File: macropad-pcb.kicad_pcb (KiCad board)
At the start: 2 copper layers, 75 x 35 mm, 12 parts

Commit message: rev2 ready for sleeping on
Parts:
- removed G***: LOGO, ct-kicad:awesome-logo
- removed MAIN: HC-FPC-05-10-16RLTAG, ct-kicad:FPC-SMD_16P-P0.50_HCTL_HC-FPC-05-10-16RLTAG
- added J1: Conn_01x01_Socket, Connector_PinHeader_2.54mm:PinHeader_1x01_P2.54mm_Vertical, F.Cu at (176.9, 106.0)
- added J10: Conn_01x01_Socket, Connector_PinHeader_2.54mm:PinHeader_1x01_P2.54mm_Vertical, F.Cu at (144.3, 102.8)
- added J2: Conn_01x01_Socket, Connector_PinHeader_2.54mm:PinHeader_1x01_P2.54mm_Vertical, F.Cu at (157.6, 102.2)
- added J3: Conn_01x01_Socket, Connector_PinHeader_2.54mm:PinHeader_1x01_P2.54mm_Vertical, F.Cu at (136.0, 102.0)
- added J4: Conn_01x01_Socket, Connector_PinHeader_2.54mm:PinHeader_1x01_P2.54mm_Vertical, F.Cu at (121.5, 102.0)
- added J5: Conn_01x01_Socket, Connector_PinHeader_2.54mm:PinHeader_1x01_P2.54mm_Vertical, F.Cu at (151.7, 102.8)
- added J6: Conn_01x01_Socket, Connector_PinHeader_2.54mm:PinHeader_1x01_P2.54mm_Vertical, F.Cu at (117.5, 96.5)
- added J7: Conn_01x01_Socket, Connector_PinHeader_2.54mm:PinHeader_1x01_P2.54mm_Vertical, F.Cu at (117.5, 103.4)
- added J8: Conn_01x01_Socket, Connector_PinHeader_2.54mm:PinHeader_1x01_P2.54mm_Vertical, F.Cu at (175.8, 94.8)
- added J9: Conn_01x01_Socket, Connector_PinHeader_2.54mm:PinHeader_1x01_P2.54mm_Vertical, F.Cu at (148.0, 102.8)
- added LOGO1: **REF, ct-kicad:awesome-logo, F.Cu at (140.6, 99.3)
- added LOGO2: **REF, ct-kicad:qmk-lite, B.Cu at (147.8, 100.0)
- added MAIN1: HC-FPC-05-10-16RLTAG, ct-kicad:FPC-SMD_16P-P0.50_HCTL_HC-FPC-05-10-16RLTAG, F.Cu at (174.0, 100.0)
- H1, H2: footprint MountingHole:MountingHole_3mm -> MountingHole:MountingHole_3mm_Pad_Via
- moved R9C8 90.0 mm to (174.3, 110.9), turned to 90 degrees
- moved R8C8 90.0 mm to (174.3, 88.9), turned to 90 degrees
- moved R9C11 76.1 mm to (120.3, 110.9), turned to 90 degrees
- moved R8C11 75.7 mm to (120.3, 88.9), turned to 90 degrees
- moved R8C9 64.9 mm to (156.3, 88.9), turned to 90 degrees
- moved R9C9 64.9 mm to (156.3, 110.9), turned to 90 degrees
- moved R9C10 58.5 mm to (138.3, 110.9), turned to 90 degrees
- moved H1 58.5 mm to (130.0, 100.0)
- moved H2 58.5 mm to (165.0, 100.0)
- moved R8C10 58.4 mm to (138.3, 88.9), turned to 90 degrees
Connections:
- R8C10 pad 1: Net-(P3-Pad11) -> row8
- R8C10 pad 10: GND -> VCC
- R8C10 pad 11: Net-(P5-Pad11) -> VCC
- R8C10 pad 12: col10 -> VCC
- R8C10 pad 13: row8 -> Net-(R8C10-Pad13)
- R8C10 pad 14: unconnected-(P5-Pad14) -> GND
- R8C10 pad 15: unconnected-(P5-Pad15) -> GND
- R8C10 pad 2: VCC -> col10
- R8C10 pad 3: VCC -> Net-(R8C10-Pad3)
- R8C10 pad 4: VCC -> GND
- R8C10 pad 5: VCC -> GND
- R8C10 pad 9: GND -> VCC
- R8C11 pad 1: Net-(P5-Pad11) -> row8
- R8C11 pad 10: GND -> VCC
- R8C11 pad 11: from_row_9_DO -> VCC
- R8C11 pad 12: col11 -> VCC
- R8C11 pad 13: row8 -> Net-(R8C10-Pad3)
- R8C11 pad 14: unconnected-(P7-Pad14) -> GND
- R8C11 pad 15: unconnected-(P7-Pad15) -> GND
- R8C11 pad 2: VCC -> col11
- R8C11 pad 3: VCC -> from_row_9_DO
- R8C11 pad 4: VCC -> GND
- R8C11 pad 5: VCC -> GND
- R8C11 pad 9: GND -> VCC
- R8C8 pad 1: Net-(P1-Pad1) -> row8
- R8C8 pad 10: GND -> VCC
- R8C8 pad 11: Net-(P1-Pad11) -> VCC
- R8C8 pad 12: col8 -> VCC
- R8C8 pad 13: row8 -> LED_DI
- R8C8 pad 14: unconnected-(P1-Pad14) -> GND
- R8C8 pad 15: unconnected-(P1-Pad15) -> GND
- R8C8 pad 2: VCC -> col8
- R8C8 pad 3: VCC -> Net-(R8C8-Pad3)
- R8C8 pad 4: VCC -> GND
- R8C8 pad 5: VCC -> GND
- R8C8 pad 9: GND -> VCC
- R8C9 pad 1: Net-(P1-Pad11) -> row8
- R8C9 pad 10: GND -> VCC
- R8C9 pad 11: Net-(P3-Pad11) -> VCC
- R8C9 pad 12: col9 -> VCC
- R8C9 pad 13: row8 -> Net-(R8C8-Pad3)
- R8C9 pad 14: unconnected-(P3-Pad14) -> GND
- R8C9 pad 15: unconnected-(P3-Pad15) -> GND
- R8C9 pad 2: VCC -> col9
- R8C9 pad 3: VCC -> Net-(R8C10-Pad13)
- R8C9 pad 4: VCC -> GND
- R8C9 pad 5: VCC -> GND
- R8C9 pad 9: GND -> VCC
- R9C10 pad 1: Net-(P4-Pad11) -> row9
- R9C10 pad 10: GND -> VCC
- R9C10 pad 11: Net-(P6-Pad11) -> VCC
- R9C10 pad 12: col10 -> VCC
- R9C10 pad 13: row9 -> Net-(R9C10-Pad13)
- R9C10 pad 14: unconnected-(P6-Pad14) -> GND
- R9C10 pad 15: unconnected-(P6-Pad15) -> GND
- R9C10 pad 2: VCC -> col10
- R9C10 pad 3: VCC -> Net-(R9C10-Pad3)
- R9C10 pad 4: VCC -> GND
- R9C10 pad 5: VCC -> GND
- R9C10 pad 9: GND -> VCC
- R9C11 pad 1: Net-(P6-Pad11) -> row9
- R9C11 pad 10: GND -> VCC
- R9C11 pad 11: LED_DO_MACRO -> VCC
- R9C11 pad 12: col11 -> VCC
- R9C11 pad 13: row9 -> Net-(R9C10-Pad3)
- R9C11 pad 14: unconnected-(P8-Pad14) -> GND
- R9C11 pad 15: unconnected-(P8-Pad15) -> GND
- R9C11 pad 2: VCC -> col11
- R9C11 pad 3: VCC -> LED_DO_MACRO
- R9C11 pad 4: VCC -> GND
- R9C11 pad 5: VCC -> GND
- R9C11 pad 9: GND -> VCC
- R9C8 pad 1: from_row_9_DO -> row9
- R9C8 pad 10: GND -> VCC
- R9C8 pad 11: Net-(P2-Pad11) -> VCC
- R9C8 pad 12: col8 -> VCC
- R9C8 pad 13: row9 -> from_row_9_DO
- R9C8 pad 14: unconnected-(P2-Pad14) -> GND
- R9C8 pad 15: unconnected-(P2-Pad15) -> GND
- R9C8 pad 2: VCC -> col8
- R9C8 pad 3: VCC -> Net-(R9C8-Pad3)
- R9C8 pad 4: VCC -> GND
- R9C8 pad 5: VCC -> GND
- R9C8 pad 9: GND -> VCC
- R9C9 pad 1: Net-(P2-Pad11) -> row9
- R9C9 pad 10: GND -> VCC
- R9C9 pad 11: Net-(P4-Pad11) -> VCC
- R9C9 pad 12: col9 -> VCC
- R9C9 pad 13: row9 -> Net-(R9C8-Pad3)
- R9C9 pad 14: unconnected-(P4-Pad14) -> GND
- R9C9 pad 15: unconnected-(P4-Pad15) -> GND
- R9C9 pad 2: VCC -> col9
- R9C9 pad 3: VCC -> Net-(R9C10-Pad13)
- R9C9 pad 4: VCC -> GND
- R9C9 pad 5: VCC -> GND
- R9C9 pad 9: GND -> VCC
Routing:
- net GND: track 38.7 -> 251.9 mm, vias 0 -> 34
- net Net-(P1-Pad1): track 47.0 -> 0.00 mm, vias 2 -> 0
- net Net-(R9C10-Pad3): track 0.00 -> 39.1 mm, vias 0 -> 8
- net Net-(R8C10-Pad3): track 0.00 -> 38.6 mm, vias 0 -> 6
- net Net-(P4-Pad11): track 31.2 -> 0.00 mm, vias 4 -> 0
- net Net-(P2-Pad11): track 29.7 -> 0.00 mm, vias 2 -> 0
- net VCC: track 238.4 -> 209.0 mm, vias 10 -> 15
- net Net-(P6-Pad11): track 29.3 -> 0.00 mm, vias 2 -> 0
- net Net-(P3-Pad11): track 29.2 -> 0.00 mm, vias 4 -> 0
- net Net-(P1-Pad11): track 28.8 -> 0.00 mm, vias 2 -> 0
- net Net-(R9C8-Pad3): track 0.00 -> 28.5 mm, vias 0 -> 6
- net LED_DO_MACRO: track 44.7 -> 73.0 mm, vias 4 -> 8
- net Net-(R9C10-Pad13): track 0.00 -> 28.3 mm, vias 0 -> 4
- net Net-(P5-Pad11): track 27.4 -> 0.00 mm, vias 2 -> 0
- net Net-(R8C8-Pad3): track 0.00 -> 24.7 mm, vias 0 -> 6
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- added copper zone on B.Cu, net GND
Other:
- board size 75 x 35 mm -> 65 x 30 mm
- board text added: "5v"
- board text added: "C10"
- board text added: "C11"
- board text added: "C8"
- board text added: "C9"
- board text added: "Compli-keeb-inator"
- board text added: "DI"
- board text added: "DO"
- board text added: "Gn"
- board text added: "R8"
- board text added: "R9"
- board text removed: "FFC cables req'd: 1x 0.5mm-pitch 16-pin 8x 0.3mm-pitch 13-pin"
- board text removed: "Mounting: M3, 35mm center-to-center"
- board text removed: "mk19-Macropad Cyboard breakout v1.0"

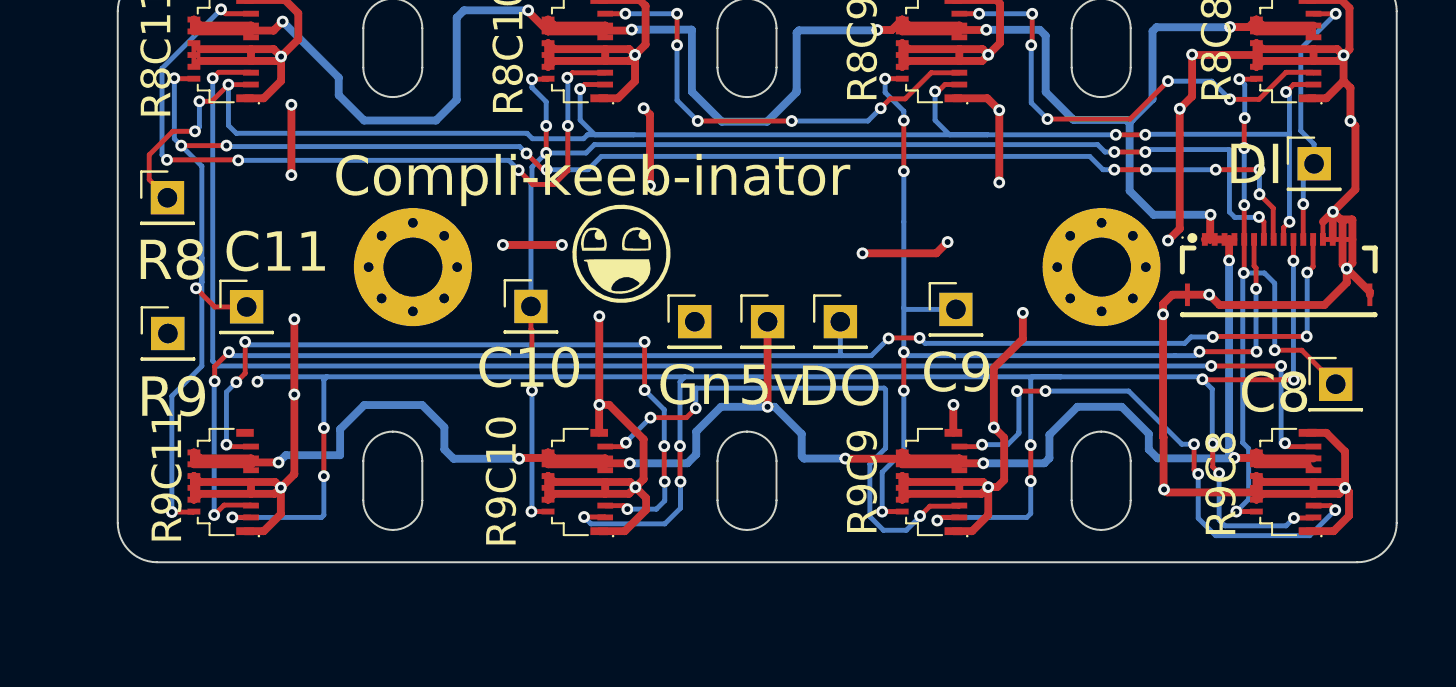
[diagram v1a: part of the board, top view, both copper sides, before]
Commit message: more updates to the board, waiting on cyboard logo
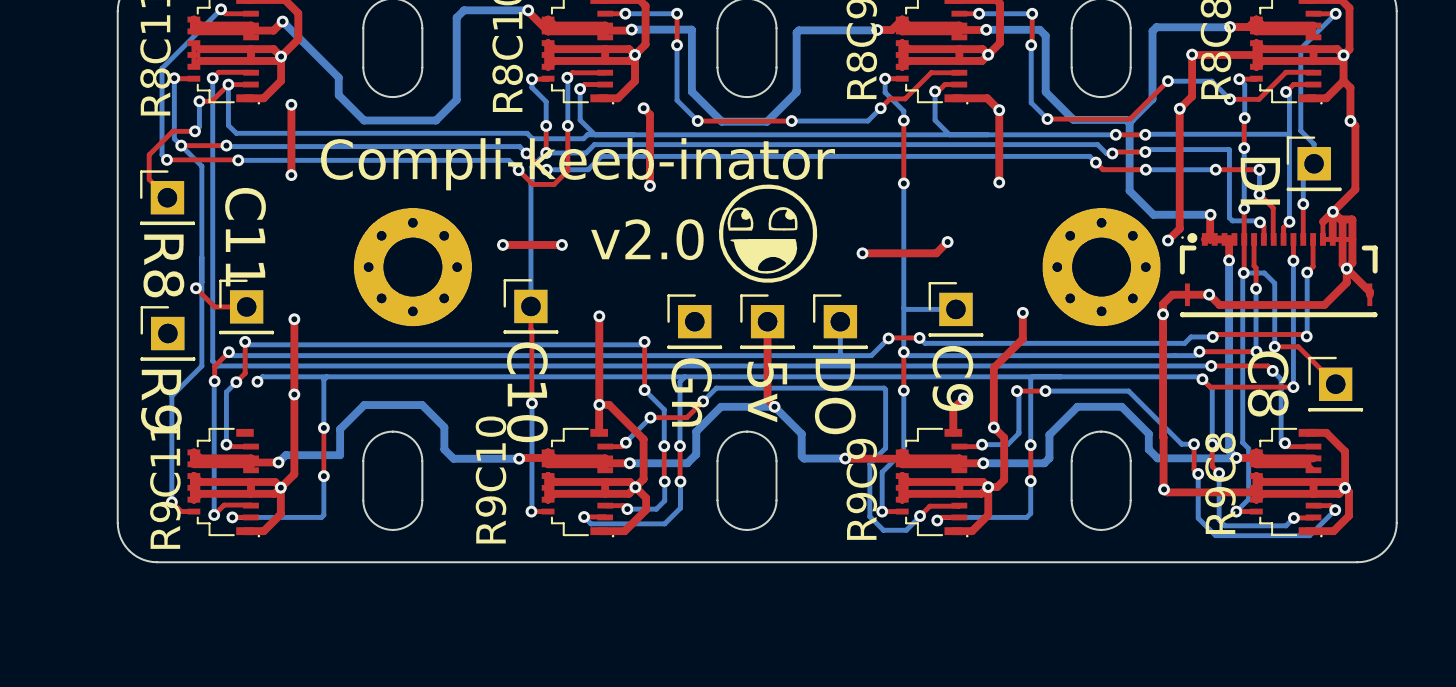
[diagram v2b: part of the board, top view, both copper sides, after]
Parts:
- added LOGO3: **REF, ct-kicad:awesome-logo, B.Cu at (123.3, 98.1)
- added LOGO4: **REF, ct-kicad:macropad-pcb-qr-10mm, B.Cu at (142.4, 96.4)
- moved LOGO2 8.18 mm to (142.0, 105.8)
- moved LOGO1 7.52 mm to (148.1, 98.3)
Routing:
- net Net-(R9C10-Pad13): track 28.3 -> 27.7 mm
- net GND: track 251.9 -> 252.5 mm
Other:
- board text added: "Compli- keeb- inator"
- board text added: "v2.0"

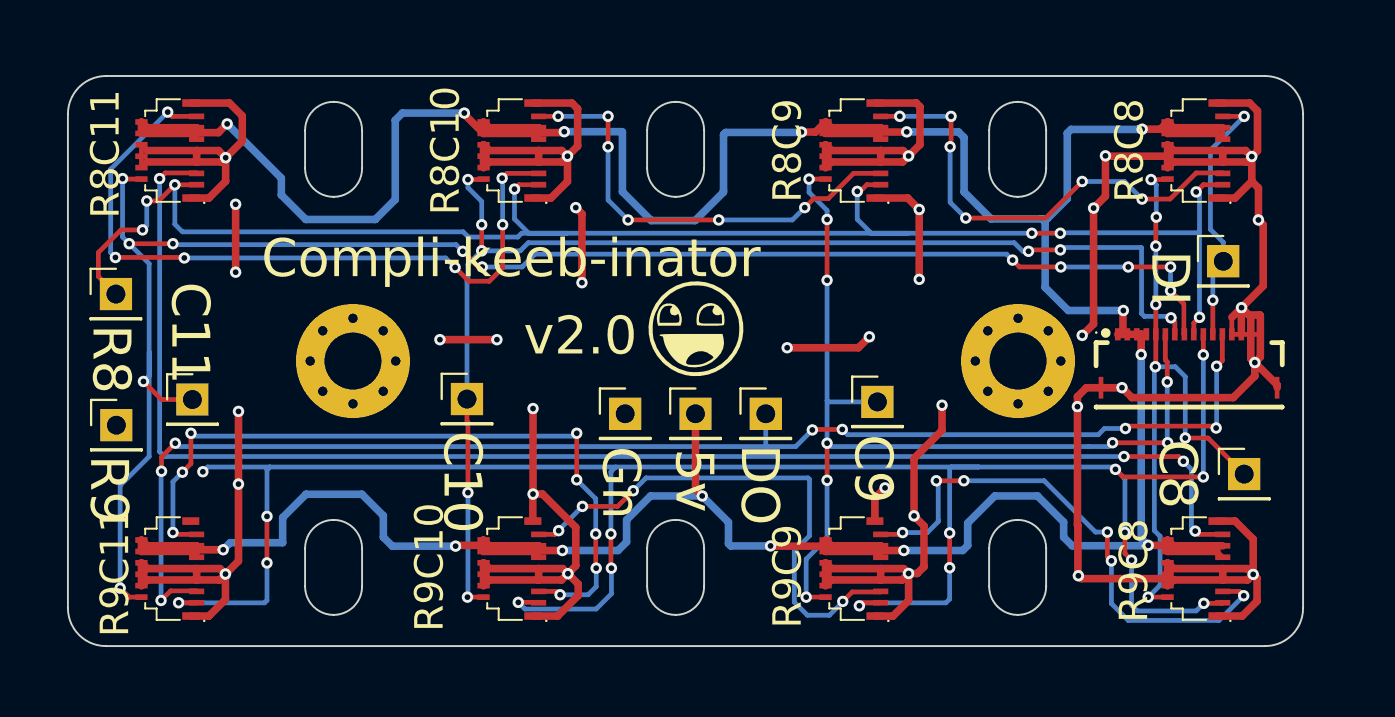
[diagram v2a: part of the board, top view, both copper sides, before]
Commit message: updated w. flipped main connectior
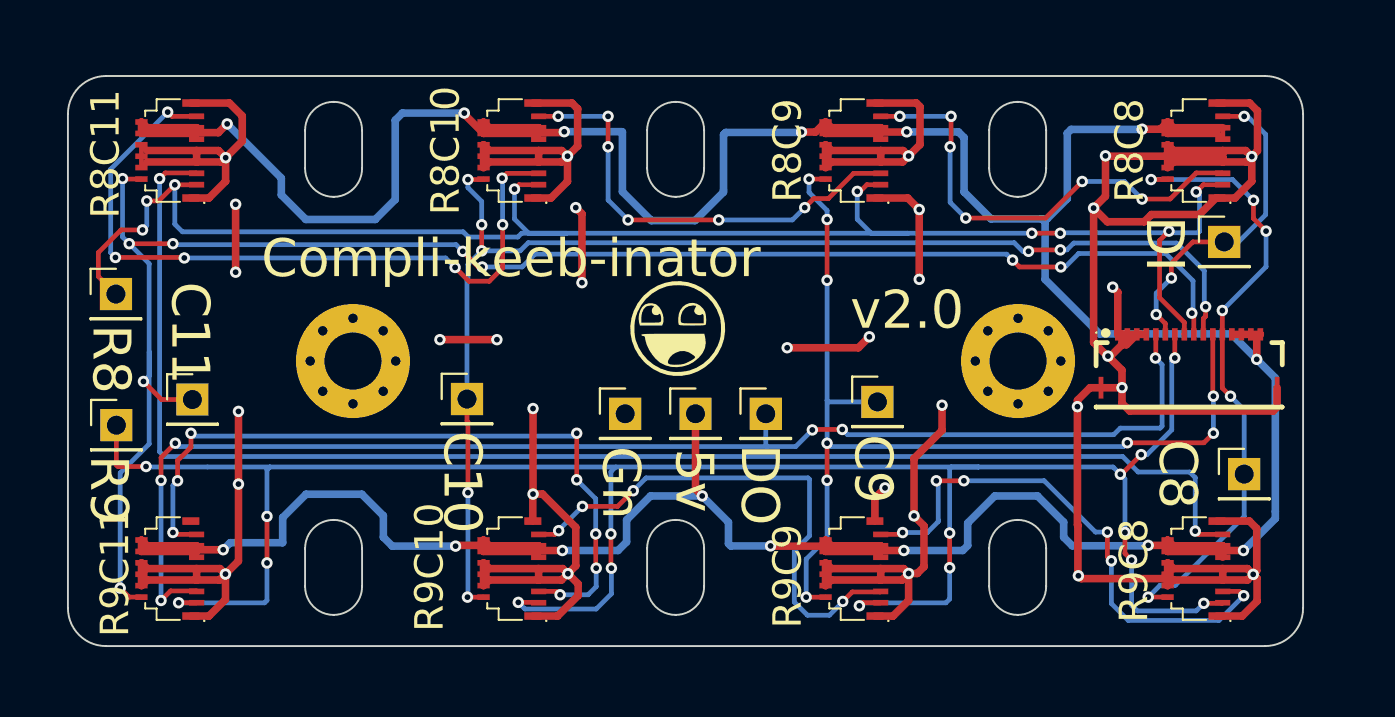
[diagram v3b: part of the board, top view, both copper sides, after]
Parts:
- moved LOGO4 6.83 mm to (137.4, 91.7)
- moved J8 1.02 mm to (175.8, 93.7)
- moved LOGO1 0.96 mm to (147.1, 98.3)
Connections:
- MAIN1 pad 1: VCC -> GND
- MAIN1 pad 10: row9 -> col10
- MAIN1 pad 11: LED_DI -> col9
- MAIN1 pad 12: LED_DO_MACRO -> col8
- MAIN1 pad 13: GND -> VCC
- MAIN1 pad 14: GND -> VCC
- MAIN1 pad 15: GND -> VCC
- MAIN1 pad 16: GND -> VCC
- MAIN1 pad 2: VCC -> GND
- MAIN1 pad 3: VCC -> GND
- MAIN1 pad 4: VCC -> GND
- MAIN1 pad 5: col8 -> LED_DO_MACRO
- MAIN1 pad 6: col9 -> LED_DI
- MAIN1 pad 7: col10 -> row9
- MAIN1 pad 8: col11 -> row8
- MAIN1 pad 9: row8 -> col11
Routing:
- net VCC: track 209.1 -> 218.7 mm
- net LED_DI: track 13.8 -> 17.2 mm, vias 2 -> 3
- net row9: track 113.5 -> 116.6 mm
- net LED_DO_MACRO: track 73.1 -> 70.1 mm, vias 8 -> 6
- net GND: track 252.5 -> 254.7 mm, vias 34 -> 32
- net col9: track 51.3 -> 53.3 mm
- net col10: track 65.6 -> 67.0 mm
- net col11: track 89.4 -> 90.6 mm, vias 12 -> 10
- net row8: track 87.4 -> 88.1 mm
- net col8: track 33.3 -> 32.9 mm, vias 7 -> 6
- net from_row_9_DO: track 76.1 -> 75.9 mm, vias 4 -> 2

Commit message: added cyboard logo
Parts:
- added LOGO5: **REF, ct-kicad:cyboard-logo-10mm, B.Cu at (174.0, 99.1)
